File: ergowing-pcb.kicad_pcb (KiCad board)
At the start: 2 copper layers, 150 parts, among them J1 USB_mini_micro_B, K0:0 KEYSW, K0:1 KEYSW, K0:2 KEYSW, K0:3 KEYSW, K0:4 KEYSW, K10:0 KEYSW, K10:1 KEYSW, K10:2 KEYSW, K10:3 KEYSW, K10:4 KEYSW, K11:0 KEYSW, K11:1 KEYSW, K11:2 KEYSW, K11:3 KEYSW, K11:4 KEYSW, K12:0 KEYSW, K12:1 KEYSW, K12:2 KEYSW, K12:3 KEYSW, K12:4 KEYSW, K13:0 KEYSW, K13:1 KEYSW, K13:2 KEYSW, K13:3 KEYSW, K13:4 KEYSW, K1:0 KEYSW, K1:1 KEYSW, K1:2 KEYSW, K1:3 KEYSW, K1:4 KEYSW, K2:0 KEYSW, K2:1 KEYSW, K2:2 KEYSW, K2:3 KEYSW, K2:4 KEYSW, K3:0 KEYSW, K3:1 KEYSW, K3:2 KEYSW, K3:3 KEYSW, K3:4 KEYSW, K4:0 KEYSW, K4:1 KEYSW, K4:2 KEYSW, K4:3 KEYSW, K4:4 KEYSW, K5:0 KEYSW, K5:1 KEYSW, K5:2 KEYSW, K5:3 KEYSW, K5:4 KEYSW, K6:0 KEYSW, K6:1 KEYSW, K6:3 KEYSW, K7:0 KEYSW, K7:1 KEYSW, K7:3 KEYSW, K7:4 KEYSW, K8:0 KEYSW, K8:1 KEYSW, K8:2 KEYSW, K8:3 KEYSW, K8:4 KEYSW, K9:0 KEYSW, K9:1 KEYSW, K9:2 KEYSW, K9:3 KEYSW, K9:4 KEYSW, SW1 SW_PUSH, U1 ATMEGA32U4, X1 XTAL_GND

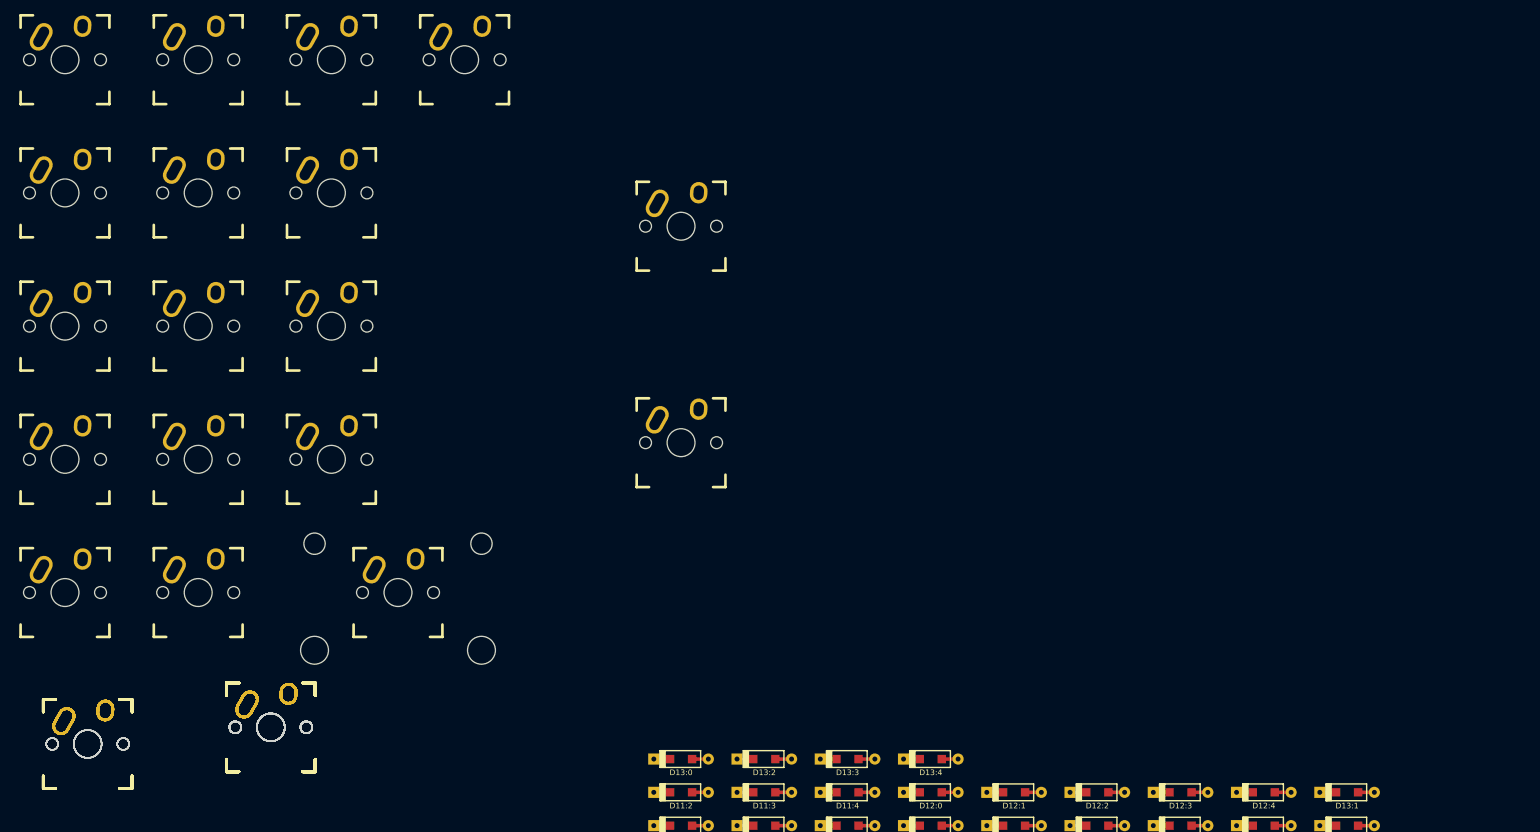
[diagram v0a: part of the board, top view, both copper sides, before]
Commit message: Key switches laid out
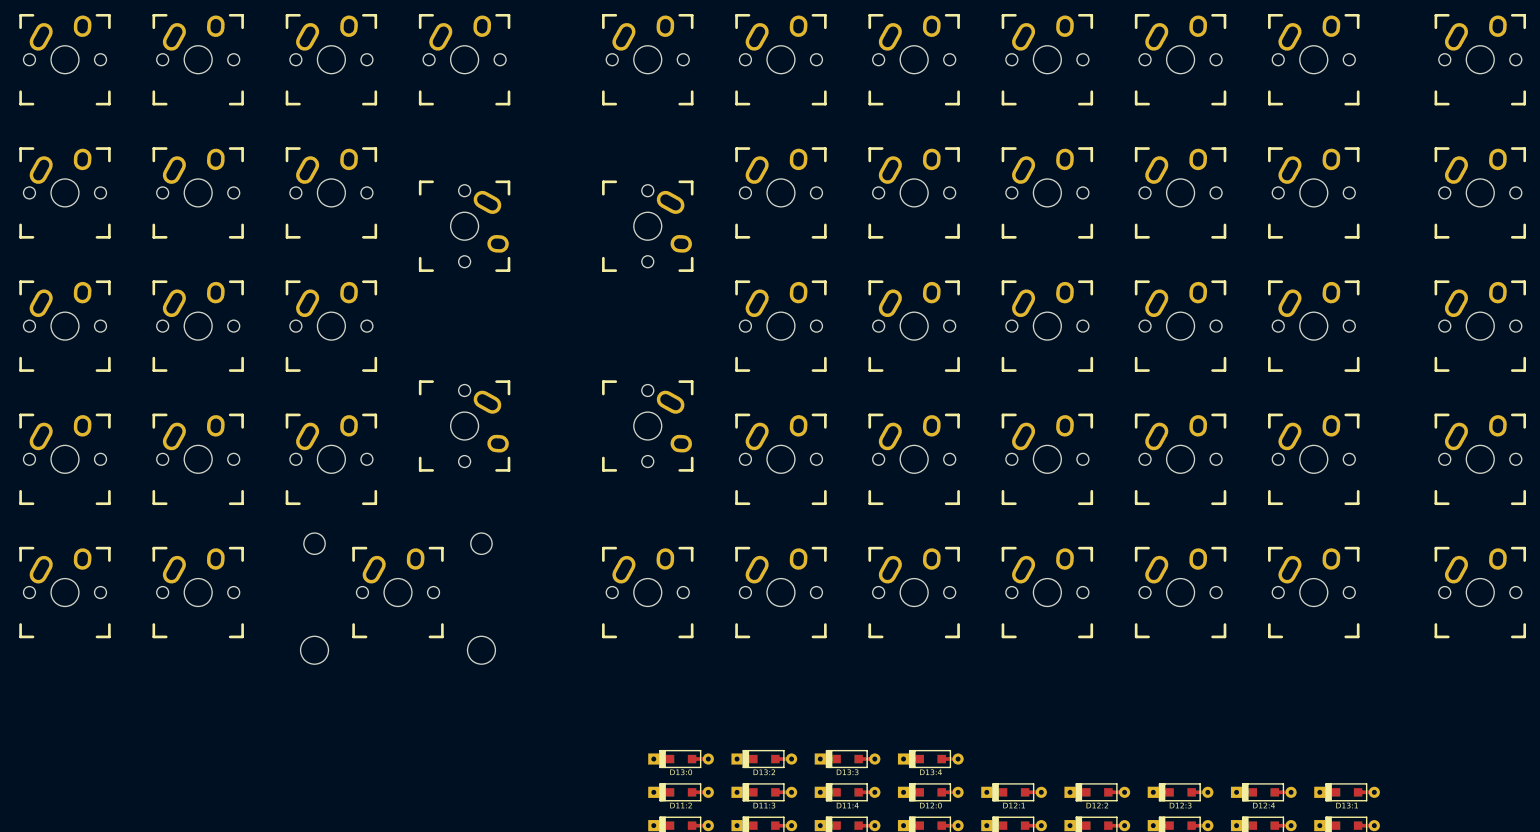
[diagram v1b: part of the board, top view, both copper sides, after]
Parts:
- moved K13:0 221.9 mm to (297.7, 28.6)
- moved K13:1 214.2 mm to (297.7, 47.6)
- moved K13:2 207.9 mm to (297.7, 66.7)
- moved K13:3 203.3 mm to (297.7, 85.7)
- moved K13:4 200.3 mm to (297.7, 104.8)
- moved K12:0 177.1 mm to (273.8, 28.6)
- moved K12:1 167.6 mm to (273.8, 47.6)
- moved K11:0 161.4 mm to (254.8, 28.6)
- moved K12:2 159.8 mm to (273.8, 66.7)
- moved K12:3 154.0 mm to (273.8, 85.7)
- moved K11:1 150.9 mm to (254.8, 47.6)
- moved K12:4 150.4 mm to (273.8, 104.8)
- moved K10:0 146.5 mm to (235.7, 28.6)
- moved K11:2 142.2 mm to (254.8, 66.7)
- moved K11:3 135.6 mm to (254.8, 85.7)
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
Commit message: Move keyswitch labels
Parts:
- C1, C2, C3, C4, C5, C6, C7, C8, D0:0, D0:1, D0:2, D0:3, D0:4, D10:0, D10:1, D10:2, D10:3, D10:4, D11:0, D11:1, D11:2, D11:3, D11:4, D12:0, D12:1, D12:2, D12:3, D12:4, D13:0, D13:1, D13:2, D13:3, D13:4, D1:0, D1:1, D1:2, D1:3, D1:4, D2:0, D2:1, D2:2, D2:3, D2:4, D3:0, D3:1, D3:2, D3:3, D3:4, D4:0, D4:1, D4:2, D4:3, D4:4, D5:0, D5:1, D5:2, D5:3, D5:4, D6:0, D6:1, D6:3, D7:0, D7:1, D7:3, D7:4, D8:0, D8:1, D8:2, D8:3, D8:4, D9:0, D9:1, D9:2, D9:3, D9:4, J1, R1, R2, R3, R4, SW1, U1, X1: moved to B.Cu
- moved D0:0 154.2 mm to (33.3, 126.2)
- moved D1:0 154.2 mm to (45.2, 126.2)
- moved D2:0 154.2 mm to (57.1, 126.2)
- moved D3:0 154.2 mm to (69.1, 126.2)
- moved D4:0 154.2 mm to (81.0, 126.2)
- moved D5:0 154.2 mm to (92.9, 126.2)
- moved D6:0 154.2 mm to (104.8, 126.2)
- moved D7:3 154.2 mm to (116.7, 126.2)
- moved D8:3 154.2 mm to (128.6, 126.2)
- moved D13:0 153.2 mm to (33.3, 159.5)
- moved D13:2 153.2 mm to (45.2, 159.5)
- moved D13:3 153.2 mm to (57.1, 159.5)
- moved D13:4 153.2 mm to (69.1, 159.5)
- moved D0:1 152.3 mm to (33.3, 131.0)
- moved D1:1 152.3 mm to (45.2, 131.0)
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
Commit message: Place diodes
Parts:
- moved D13:0 292.9 mm to (297.7, 33.3)
- moved D13:2 267.3 mm to (297.7, 71.4)
- moved D13:3 250.2 mm to (297.7, 90.5)
- moved D12:0 238.1 mm to (273.8, 33.3)
- moved D11:2 236.6 mm to (254.8, 71.4)
- moved D13:4 234.0 mm to (297.7, 109.5)
- moved D11:3 219.2 mm to (254.8, 90.5)
- moved D12:1 218.4 mm to (273.8, 52.4)
- moved D10:0 213.3 mm to (235.7, 33.3)
- moved D11:4 202.8 mm to (254.8, 109.5)
- moved D12:2 199.2 mm to (273.8, 71.4)
- moved D13:1 197.7 mm to (297.7, 52.4)
- moved D10:1 193.2 mm to (235.7, 52.4)
- moved D9:3 192.8 mm to (216.7, 90.5)
- moved D12:3 180.9 mm to (273.8, 90.5)
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
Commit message: Layout near completion
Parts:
- K0:0, K0:1, K0:2, K0:3, K0:4: footprint keebs:Mx_Alps_150 -> keebs:Mx_Alps_150_R-5deg
- K10:0, K10:1, K10:2, K10:3, K10:4, K11:0, K11:1, K11:2, K11:3, K11:4, K12:0, K12:1, K12:2, K12:3, K12:4, K7:0, K7:4, K8:0, K8:1, K8:2, K8:3, K8:4, K9:0, K9:1, K9:2, K9:3, K9:4: footprint keebs:Mx_Alps_100 -> keebs:Mx_Alps_100_R5deg
- K13:0, K13:1, K13:2, K13:3, K13:4: footprint keebs:Mx_Alps_150 -> keebs:Mx_Alps_150_R5deg
- K1:0, K1:1, K1:2, K1:3, K1:4, K2:0, K2:1, K2:2, K2:3, K2:4, K3:0, K3:1, K3:2, K3:3, K3:4, K4:0, K4:1, K4:2, K4:3, K4:4, K5:0, K5:1, K5:2, K5:3, K6:0: footprint keebs:Mx_Alps_100 -> keebs:Mx_Alps_100_R-5deg
- moved D7:3 279.4 mm to (257.2, 347.7)
- moved D7:1 279.4 mm to (257.2, 319.1)
- moved D5:4 270.9 mm to (190.5, 376.2)
- moved D6:3 270.9 mm to (195.3, 347.7)
- moved D6:1 270.9 mm to (195.3, 319.1)
- moved D11:4 190.8 mm to (347.7, 276.2)
- moved D10:0 190.8 mm to (328.6, 200.0)
- moved D10:1 190.8 mm to (328.6, 219.1)
- moved D10:2 190.8 mm to (328.6, 238.1)
- moved D10:3 190.8 mm to (328.6, 257.2)
- moved D10:4 190.8 mm to (328.6, 276.2)
- moved D11:0 190.8 mm to (347.7, 200.0)
- moved D11:1 190.8 mm to (347.7, 216.7)
- moved D11:2 190.8 mm to (347.7, 238.1)
- moved D11:3 190.8 mm to (347.7, 257.2)
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
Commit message: Layout near completion #2
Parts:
- moved K11:0 15.8 mm to (277.8, 43.5)
- moved K12:0 15.8 mm to (296.5, 41.8)
- moved K13:2 15.8 mm to (323.3, 77.2)
- moved K9:2 15.8 mm to (245.3, 102.9)
- moved K9:4 15.8 mm to (246.9, 121.6)
- moved K8:2 15.8 mm to (224.9, 85.8)
- moved K8:3 15.8 mm to (226.6, 104.5)
- moved K9:3 15.8 mm to (243.7, 84.2)
- moved K10:0 15.8 mm to (259.2, 45.1)
- moved K10:3 15.8 mm to (264.0, 101.2)
- moved K11:1 15.8 mm to (279.5, 62.2)
- moved K11:3 15.8 mm to (282.8, 99.6)
- moved K11:4 15.8 mm to (284.4, 118.4)
- moved K12:1 15.8 mm to (298.2, 60.5)
- moved K12:2 15.8 mm to (299.8, 79.3)
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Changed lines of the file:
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@@
     (links 515)
     (no_connects 247)
-    (area -15.201906 -10.872608 395.425 383.7146)
+    (area 43.748094 28.857392 395.425 379.0775)
     (thickness 1.6)
     (drawings 0)
@@
   )
   (module keebs:Mx_Alps_150 (layer F.Cu)
-    (at 220.39 77.06 275)
+    (at 205 73.49 275)
     (descr MXALPS)
     (tags MXALPS)
@@
   )
   (module keebs:Mx_Alps_150 (layer F.Cu)
-    (at 222.85 105 275)
+    (at 207.46 101.43 275)
     (descr MXALPS)
     (tags MXALPS)
@@
   )
   (module keebs:Mx_Alps_100_R5deg (layer F.Cu)
-    (at 218.35 53.53)
+    (at 202.96 49.96)
     (descr MXALPS)
     (tags MXALPS)
@@
   )
   (module keebs:Mx_Alps_100_R5deg (layer F.Cu)
-    (at 224.94 128.44)
+    (at 209.55 124.87)
     (descr MXALPS)
     (tags MXALPS)
@@
   )
   (module keebs:Mx_Alps_100_R5deg (layer F.Cu)
-    (at 237.04 51.91)
+    (at 221.65 48.34)
     (descr MXALPS)
     (tags MXALPS)
@@
   )
   (module keebs:Mx_Alps_100_R5deg (layer F.Cu)
-    (at 238.69 70.63)
+    (at 223.3 67.06)
     (descr MXALPS)
     (tags MXALPS)
@@
   )
   (module keebs:Mx_Alps_100_R5deg (layer F.Cu)
-    (at 240.34 89.35)
+    (at 224.95 85.78)
     (descr MXALPS)
     (tags MXALPS)
@@
   )
   (module keebs:Mx_Alps_100_R5deg (layer F.Cu)
-    (at 241.99 108.07)
+    (at 226.6 104.5)
     (descr MXALPS)
     (tags MXALPS)
@@
   )
   (module keebs:Mx_Alps_100_R5deg (layer F.Cu)
-    (at 243.64 126.79)
+    (at 228.25 123.22)
     (descr MXALPS)
     (tags MXALPS)
@@
   )
   (module keebs:Mx_Alps_100_R5deg (layer F.Cu)
-    (at 255.79 50.29)
+    (at 240.4 46.72)
     (descr MXALPS)
     (tags MXALPS)
@@
   )
   (module keebs:Mx_Alps_100_R5deg (layer F.Cu)
-    (at 257.44 69)
+    (at 242.05 65.43)
     (descr MXALPS)
     (tags MXALPS)
@@
   )
   (module keebs:Mx_Alps_100_R5deg (layer F.Cu)
-    (at 260.68 106.45)
+    (at 245.29 102.88)
     (descr MXALPS)
     (tags MXALPS)
@@
   )
   (module keebs:Mx_Alps_100_R5deg (layer F.Cu)
-    (at 259.06 87.72)
+    (at 243.67 84.15)
     (descr MXALPS)
     (tags MXALPS)
@@
   )
   (module keebs:Mx_Alps_100_R5deg (layer F.Cu)
-    (at 262.3 125.2)
+    (at 246.91 121.63)
     (descr MXALPS)
     (tags MXALPS)
@@
   )
   (module keebs:Mx_Alps_100_R5deg (layer F.Cu)
-    (at 274.55 48.65)
+    (at 259.16 45.08)
     (descr MXALPS)
     (tags MXALPS)
@@
   )
   (module keebs:Mx_Alps_100_R5deg (layer F.Cu)
-    (at 276.19 67.38)
+    (at 260.8 63.81)
     (descr MXALPS)
     (tags MXALPS)
@@
   )
   (module keebs:Mx_Alps_100_R5deg (layer F.Cu)
-    (at 277.82 86.1)
+    (at 262.43 82.53)
     (descr MXALPS)
     (tags MXALPS)
@@
   )
   (module keebs:Mx_Alps_100_R5deg (layer F.Cu)
-    (at 279.43 104.81)
+    (at 264.04 101.24)
     (descr MXALPS)
     (tags MXALPS)
@@
   )
   (module keebs:Mx_Alps_100_R5deg (layer F.Cu)
-    (at 281.08 123.55)
+    (at 265.69 119.98)
     (descr MXALPS)
     (tags MXALPS)
@@
   )
   (module keebs:Mx_Alps_100_R5deg (layer F.Cu)
-    (at 293.22 47.02)
+    (at 277.83 43.45)
     (descr MXALPS)
     (tags MXALPS)
@@
   )
   (module keebs:Mx_Alps_100_R5deg (layer F.Cu)
-    (at 294.86 65.76)
+    (at 279.47 62.19)
     (descr MXALPS)
     (tags MXALPS)
@@
   )
   (module keebs:Mx_Alps_100_R5deg (layer F.Cu)
-    (at 296.5 84.46)
+    (at 281.11 80.89)
     (descr MXALPS)
     (tags MXALPS)
@@
   )
   (module keebs:Mx_Alps_100_R5deg (layer F.Cu)
-    (at 298.15 103.18)
+    (at 282.76 99.61)
     (descr MXALPS)
     (tags MXALPS)
@@
   )
   (module keebs:Mx_Alps_100_R5deg (layer F.Cu)
-    (at 299.8 121.93)
+    (at 284.41 118.36)
     (descr MXALPS)
     (tags MXALPS)
@@
   )
   (module keebs:Mx_Alps_100_R5deg (layer F.Cu)
-    (at 311.92 45.4)
+    (at 296.53 41.83)
     (descr MXALPS)
     (tags MXALPS)
@@
   )
   (module keebs:Mx_Alps_100_R5deg (layer F.Cu)
-    (at 313.57 64.12)
+    (at 298.18 60.55)
     (descr MXALPS)
     (tags MXALPS)
@@
   )
   (module keebs:Mx_Alps_100_R5deg (layer F.Cu)
-    (at 315.2 82.87)
+    (at 299.81 79.3)
     (descr MXALPS)
     (tags MXALPS)
@@
   )
   (module keebs:Mx_Alps_100_R5deg (layer F.Cu)
-    (at 318.52 120.31)
+    (at 303.13 116.74)
     (descr MXALPS)
     (tags MXALPS)
@@
   )
   (module keebs:Mx_Alps_100_R5deg (layer F.Cu)
-    (at 316.87 101.59)
+    (at 301.48 98.02)
     (descr MXALPS)
     (tags MXALPS)
@@
   )
   (module keebs:Mx_Alps_150_R5deg (layer F.Cu)
-    (at 335.39 43.32)
+    (at 320 39.75)
     (descr MXALPS)
     (tags MXALPS)
@@
   )
   (module keebs:Mx_Alps_150_R5deg (layer F.Cu)
-    (at 337.03 62.06)
+    (at 321.64 58.49)
     (descr MXALPS)
     (tags MXALPS)
@@
   )
   (module keebs:Mx_Alps_150_R5deg (layer F.Cu)
-    (at 338.67 80.81)
+    (at 323.28 77.24)
     (descr MXALPS)
     (tags MXALPS)
@@
   )
   (module keebs:Mx_Alps_150_R5deg (layer F.Cu)
-    (at 340.34 99.55)
+    (at 324.95 95.98)
     (descr MXALPS)
     (tags MXALPS)
@@
   )
   (module keebs:Mx_Alps_150_R5deg (layer F.Cu)
-    (at 341.99 118.27)
+    (at 326.6 114.7)
     (descr MXALPS)
     (tags MXALPS)
